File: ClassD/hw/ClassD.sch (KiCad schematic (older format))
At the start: 62 parts, among them P1 RedRCA, P2 WhiteRCA, P3 CONN_01X02, P4 CONN_01X02, P5 CONN_01X02, SW1 SW_PUSH, SW2 SW_PUSH, U1 TDA7491LP, U2 MCP1700T

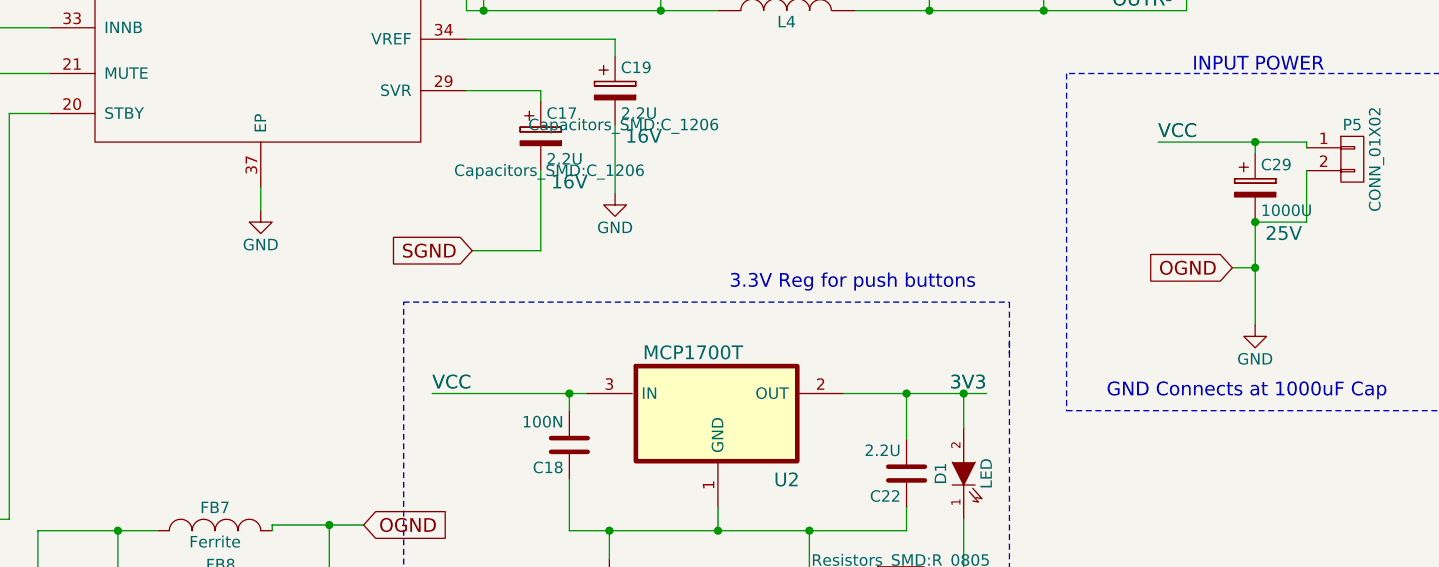
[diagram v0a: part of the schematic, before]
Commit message: Finished output filters (right side)
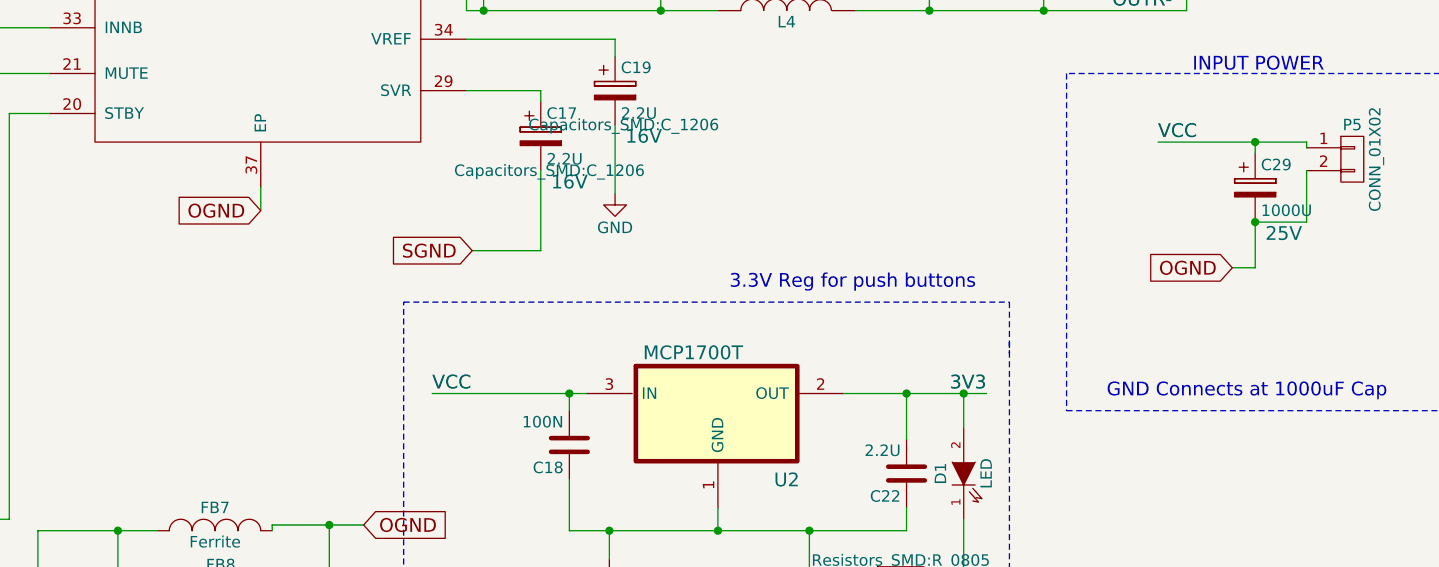
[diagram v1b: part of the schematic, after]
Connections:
- net GND: no longer C15.1, C16.2, C25.2, C26.1, C27.2, C28.1, C29.2, FB1.2, FB2.2, FB3.2, FB4.2, FB5.2, FB6.2, FB7.2, FB8.2, P5.2 (P2), U1.14 (PGNDA), U1.15 (PGNDA), U1.37 (EP), U1.4 (PGNDB), U1.5 (PGNDB)
- new net OGND: C15.1, C16.2, C25.2, C26.1, C27.2, C28.1, C29.2, FB1.2, FB2.2, FB3.2, FB4.2, FB5.2, FB6.2, FB7.2, FB8.2, P5.2 (P2), U1.14 (PGNDA), U1.15 (PGNDA), U1.37 (EP), U1.4 (PGNDB), U1.5 (PGNDB)
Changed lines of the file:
@@
 STBY
-$Comp
-L GND #PWR07
-U 1 1 56B32119
-P 5800 4650
-F 0 "#PWR07" H 5800 4400 50  0001 C CNN
-F 1 "GND" H 5800 4500 50  0000 C CNN
-F 2 "" H 5800 4650 50  0000 C CNN
-F 3 "" H 5800 4650 50  0000 C CNN
-	1    5800 4650
-	1    0    0    -1
-$EndComp
 $Comp
 L GND #PWR08
@@
 	1    0    0    -1
 $EndComp
-$Comp
-L GND #PWR09
-U 1 1 56B38442
-P 10150 5150
-F 0 "#PWR09" H 10150 4900 50  0001 C CNN
-F 1 "GND" H 10150 5000 50  0000 C CNN
-F 2 "" H 10150 5150 50  0000 C CNN
-F 3 "" H 10150 5150 50  0000 C CNN
-	1    10150 5150
-	1    0    0    -1
-$EndComp
 Text Notes 9500 5475 0    60   ~ 0
 GND Connects at 1000uF Cap
@@
 	10050 4900 10150 4900
 Wire Wire Line
-	10150 4700 10150 5150
-Wire Wire Line
 	10150 4700 10375 4700
 Wire Wire Line
 	10375 4700 10375 4475
 Connection ~ 10150 4700
-Connection ~ 10150 4900
 Wire Wire Line
 	10150 4400 10150 4350
@@
 	5175 7625 5275 7625
 Connection ~ 5175 7400
+Wire Wire Line
+	10150 4900 10150 4700
+Text GLabel 5800 4650 0    60   Input ~ 0
+OGND
 $EndSCHEMATC

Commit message: Finished layout with DRC
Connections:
- net GND: no longer U1.1 (SUB_GND)
- net OGND: now also U1.1 (SUB_GND)
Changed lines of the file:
@@
 LIBS:valves
 LIBS:ClassD
-LIBS:stm32f030c8
 LIBS:ClassD-cache
 EELAYER 25 0
@@
 $EndComp
 $Comp
-L GND #PWR01
-U 1 1 56B2E3CA
-P 4350 850
-F 0 "#PWR01" H 4350 600 50  0001 C CNN
-F 1 "GND" H 4350 700 50  0000 C CNN
-F 2 "" H 4350 850 50  0000 C CNN
-F 3 "" H 4350 850 50  0000 C CNN
-	1    4350 850
-	1    0    0    -1
-$EndComp
-$Comp
 L C C3
 U 1 1 56B2E3E6
@@
 	4875 1575 2275 1575
 Wire Wire Line
-	2275 1575 2275 1925
+	2275 1575 2275 1875
+Wire Wire Line
+	2275 1875 2275 1925
 Wire Wire Line
 	2075 1500 2075 1375
 Wire Wire Line
-	1775 1375 4875 1375
+	1775 1375 2075 1375
+Wire Wire Line
+	2075 1375 4875 1375
 Wire Wire Line
 	2275 2300 2275 2225
 Wire Wire Line
-	2075 2300 2275 2300
+	2075 2300 2175 2300
+Wire Wire Line
+	2175 2300 2275 2300
 Wire Wire Line
 	2075 2300 2075 1800
@@
 	875  2700 800  2700
 Wire Wire Line
-	4000 2000 4875 2000
+	4000 2000 4100 2000
+Wire Wire Line
+	4100 2000 4875 2000
 Wire Wire Line
 	4875 2000 4875 1975
@@
 	3700 2000 3375 2000
 Wire Wire Line
-	3375 1775 3375 2350
+	3375 1775 3375 2000
+Wire Wire Line
+	3375 2000 3375 2350
 Wire Wire Line
 	4875 1775 3375 1775
 Connection ~ 3375 2000
 Wire Wire Line
-	4100 2000 4100 2250
+	4100 2000 4100 2150
+Wire Wire Line
+	4100 2150 4100 2250
 Wire Wire Line
 	4100 2150 4350 2150
@@
 	4625 2500 4625 2725
 Wire Wire Line
-	4625 2725 4100 2725
+	4625 2725 4375 2725
+Wire Wire Line
+	4375 2725 4100 2725
 Wire Wire Line
 	4100 2725 4100 2550
@@
 	3575 3250 3575 3275
 Wire Wire Line
-	3575 3275 3800 3275
+	3575 3275 3650 3275
+Wire Wire Line
+	3650 3275 3800 3275
 Wire Wire Line
 	3800 3275 3800 3250
@@
 	3800 2925 3800 2950
 Wire Wire Line
-	3575 2925 3800 2925
+	3575 2925 3700 2925
+Wire Wire Line
+	3700 2925 3800 2925
 Wire Wire Line
 	3575 2925 3575 2950
@@
 	4425 3000 4275 3000
 Wire Wire Line
-	4275 3000 4275 3150
+	4275 3000 4275 3075
+Wire Wire Line
+	4275 3075 4275 3150
 Wire Wire Line
 	4275 3150 4425 3150
@@
 	4125 3600 4125 3525
 Wire Wire Line
-	3675 3850 3675 4225
+	3675 3850 3675 4175
+Wire Wire Line
+	3675 4175 3675 4225
 Wire Wire Line
 	3475 3800 3475 3675
@@
 	3675 4600 3675 4525
 Wire Wire Line
-	3475 4600 3675 4600
+	3475 4600 3575 4600
+Wire Wire Line
+	3575 4600 3675 4600
 Wire Wire Line
 	3475 4600 3475 4100
@@
 	4875 3850 3675 3850
 Wire Wire Line
-	3175 3675 4875 3675
+	3175 3675 3475 3675
+Wire Wire Line
+	3475 3675 4875 3675
 Wire Wire Line
 	900  4200 900  3500
@@
 	3725 5225 3725 5175
 Wire Wire Line
-	3475 5175 4400 5175
+	3475 5175 3725 5175
+Wire Wire Line
+	3725 5175 4400 5175
 Wire Wire Line
 	3175 5175 3000 5175
@@
 	3450 6050 3450 6000
 Wire Wire Line
-	3200 6000 4700 6000
+	3200 6000 3450 6000
+Wire Wire Line
+	3450 6000 4700 6000
 Wire Wire Line
 	2900 6000 2725 6000
@@
 	6825 3050 6825 2950
 Wire Wire Line
-	6700 2950 7225 2950
+	6700 2950 6825 2950
+Wire Wire Line
+	6825 2950 6975 2950
+Wire Wire Line
+	6975 2950 7225 2950
 Wire Wire Line
 	6975 2950 6975 3025
 Connection ~ 6825 2950
 Wire Wire Line
-	6975 3325 6975 3475
+	6975 3325 6975 3375
+Wire Wire Line
+	6975 3375 6975 3475
 Wire Wire Line
 	6975 3475 7025 3475
@@
 	6900 1625 6900 1700
 Wire Wire Line
-	6700 1625 7025 1625
+	6700 1625 6775 1625
+Wire Wire Line
+	6775 1625 6900 1625
+Wire Wire Line
+	6900 1625 7025 1625
 Wire Wire Line
 	6700 1725 6775 1725
@@
 Connection ~ 6900 1625
 Wire Wire Line
-	6700 2050 7225 2050
+	6700 2050 6775 2050
+Wire Wire Line
+	6775 2050 6900 2050
+Wire Wire Line
+	6900 2050 7225 2050
 Wire Wire Line
 	6700 1950 6775 1950
@@
 Connection ~ 6900 2050
 Wire Wire Line
-	9725 4350 10375 4350
+	9725 4350 10150 4350
+Wire Wire Line
+	10150 4350 10375 4350
 Wire Wire Line
 	10375 4350 10375 4375
@@
 	10150 4400 10150 4350
 Wire Wire Line
-	6700 1225 7700 1225
+	6700 1225 6950 1225
+Wire Wire Line
+	6950 1225 7675 1225
+Wire Wire Line
+	7675 1225 7700 1225
 Wire Wire Line
 	6700 1325 6950 1325
@@
 Connection ~ 7675 1225
 Wire Wire Line
-	6700 2350 7800 2350
+	6700 2350 6800 2350
+Wire Wire Line
+	6800 2350 7675 2350
+Wire Wire Line
+	7675 2350 7800 2350
 Wire Wire Line
 	6700 2350 6700 2375
@@
 $EndComp
 Wire Wire Line
-	8300 1225 9850 1225
+	8300 1225 8725 1225
+Wire Wire Line
+	8725 1225 9225 1225
+Wire Wire Line
+	9225 1225 9850 1225
 Wire Wire Line
 	8725 1225 8725 1575
@@
 	8725 1875 8725 2350
 Wire Wire Line
-	8400 2350 9850 2350
+	8400 2350 8725 2350
+Wire Wire Line
+	8725 2350 9225 2350
+Wire Wire Line
+	9225 2350 9850 2350
 Text GLabel 9450 1750 2    60   Input ~ 0
 OGND
@@
 Connection ~ 8725 1225
 Wire Wire Line
-	9225 1650 9225 1875
+	9225 1650 9225 1775
+Wire Wire Line
+	9225 1775 9225 1875
 $Comp
 L C C26
@@
 Connection ~ 7550 3775
 Wire Wire Line
-	8400 2650 9850 2650
+	8400 2650 8725 2650
+Wire Wire Line
+	8725 2650 9225 2650
+Wire Wire Line
+	9225 2650 9850 2650
 Wire Wire Line
 	8725 2650 8725 3000
@@
 	8725 3300 8725 3775
 Wire Wire Line
-	8400 3775 9850 3775
+	8400 3775 8725 3775
+Wire Wire Line
+	8725 3775 9225 3775
+Wire Wire Line
+	9225 3775 9850 3775
 Text GLabel 9450 3175 2    60   Input ~ 0
 OGND
@@
 Connection ~ 8725 2650
 Wire Wire Line
-	9225 3075 9225 3300
+	9225 3075 9225 3200
+Wire Wire Line
+	9225 3200 9225 3300
 $Comp
 L C C28
@@
 	6825 3275 6825 3375
 Wire Wire Line
-	6700 3375 6975 3375
+	6700 3375 6825 3375
+Wire Wire Line
+	6825 3375 6975 3375
 Connection ~ 6975 3375
 Connection ~ 6825 3375
@@
 	6900 2050 6900 2000
 Wire Wire Line
-	6750 2650 7800 2650
+	6750 2650 6775 2650
+Wire Wire Line
+	6775 2650 7550 2650
+Wire Wire Line
+	7550 2650 7800 2650
 Wire Wire Line
 	6750 2650 6750 2625
@@
 Connection ~ 6775 2650
 Wire Wire Line
-	6700 3775 7800 3775
+	6700 3775 6775 3775
+Wire Wire Line
+	6775 3775 7550 3775
+Wire Wire Line
+	7550 3775 7800 3775
 Wire Wire Line
 	6700 3675 6700 3775
@@
 $EndComp
 Wire Wire Line
-	6550 5450 7225 5450
+	6550 5450 7150 5450
+Wire Wire Line
+	7150 5450 7225 5450
 Wire Wire Line
 	7150 5450 7150 5525
@@
 	7150 5825 7150 6050
 Wire Wire Line
-	7150 6050 8625 6050
+	7150 6050 7325 6050
+Wire Wire Line
+	7325 6050 7800 6050
+Wire Wire Line
+	7800 6050 8200 6050
+Wire Wire Line
+	8200 6050 8625 6050
 $Comp
 L C C22
@@
 	8625 5650 8625 5450
 Wire Wire Line
-	8350 5450 8975 5450
+	8350 5450 8625 5450
+Wire Wire Line
+	8625 5450 8875 5450
+Wire Wire Line
+	8875 5450 8975 5450
 Wire Wire Line
 	8625 6050 8625 5950
@@
 $EndComp
 Wire Wire Line
-	4825 6050 5350 6050
+	4825 6050 5175 6050
+Wire Wire Line
+	5175 6050 5350 6050
 Wire Wire Line
 	4825 6050 4825 6375
@@
 OGND
 Wire Wire Line
-	6250 6025 5850 6025
+	6250 6025 6100 6025
+Wire Wire Line
+	6100 6025 5850 6025
 Wire Wire Line
 	5850 6025 5850 6050
@@
 	5875 6300 6100 6300
 Wire Wire Line
-	6100 6025 6100 7625
+	6100 6025 6100 6300
+Wire Wire Line
+	6100 6300 6100 6525
+Wire Wire Line
+	6100 6525 6100 6725
+Wire Wire Line
+	6100 6725 6100 6900
+Wire Wire Line
+	6100 6900 6100 7150
+Wire Wire Line
+	6100 7150 6100 7400
+Wire Wire Line
+	6100 7400 6100 7625
 Connection ~ 6100 6025
 Wire Wire Line
@@
 	5375 6300 5175 6300
 Wire Wire Line
-	5175 6050 5175 7625
+	5175 6050 5175 6300
+Wire Wire Line
+	5175 6300 5175 6525
+Wire Wire Line
+	5175 6525 5175 6725
+Wire Wire Line
+	5175 6725 5175 6900
+Wire Wire Line
+	5175 6900 5175 7150
+Wire Wire Line
+	5175 7150 5175 7400
+Wire Wire Line
+	5175 7400 5175 7625
 Connection ~ 5175 6050
 Wire Wire Line
@@
 Text GLabel 5800 4650 0    60   Input ~ 0
 OGND
+Text GLabel 4350 850  0    60   Input ~ 0
+OGND
 $EndSCHEMATC

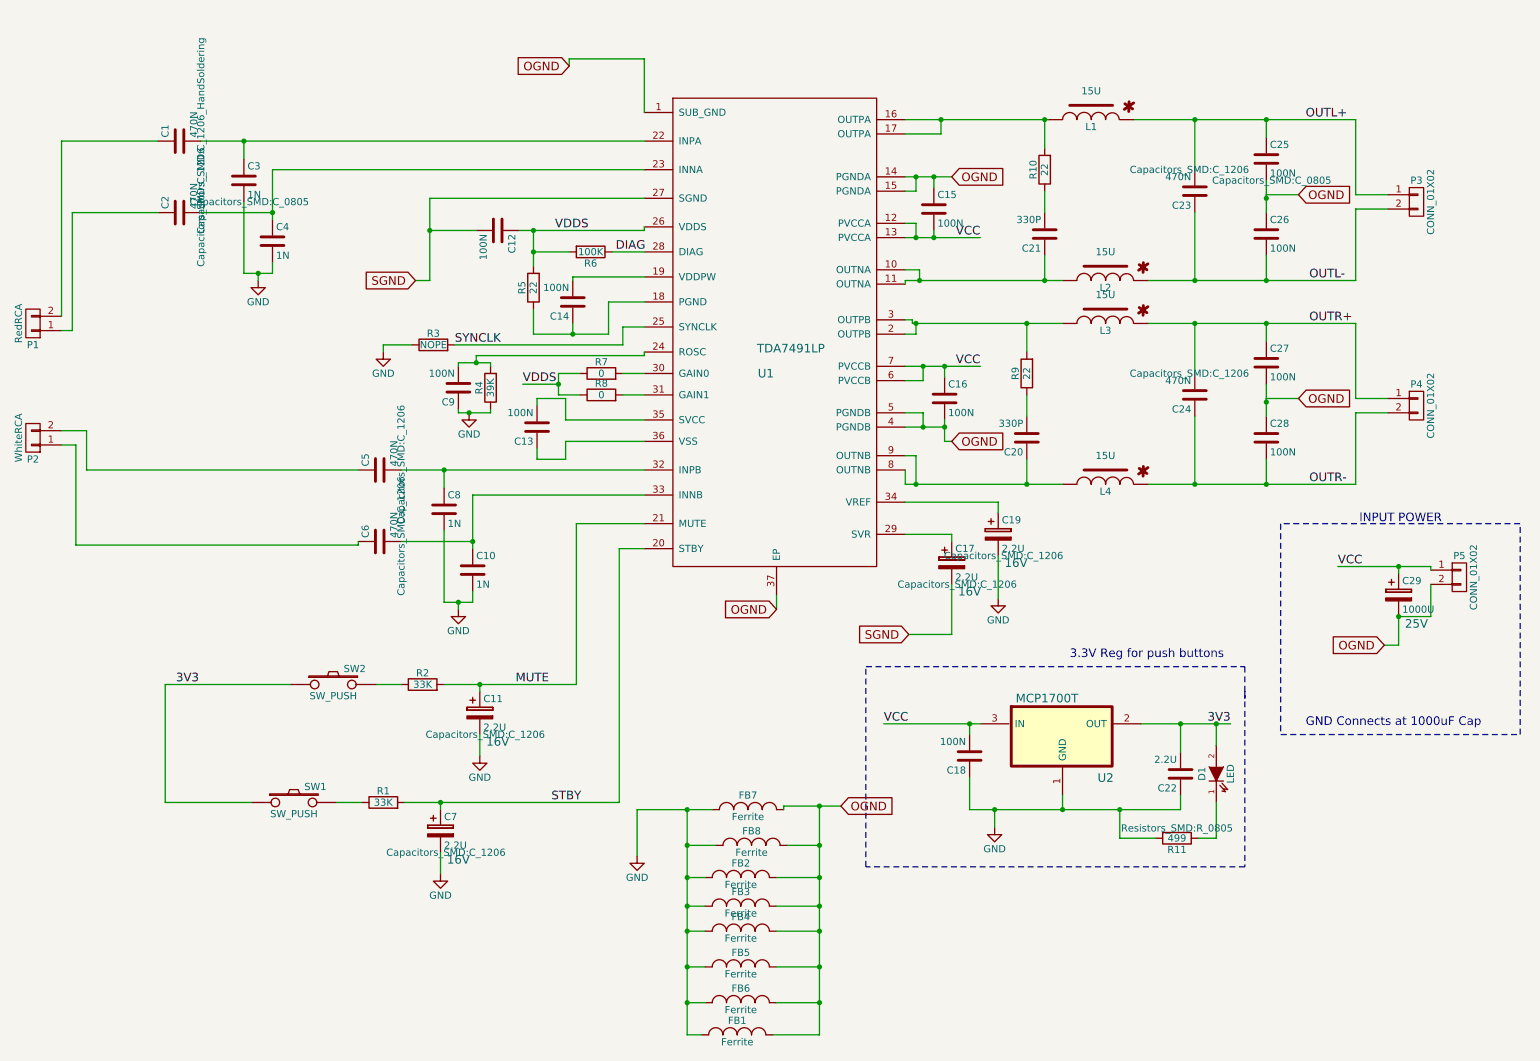
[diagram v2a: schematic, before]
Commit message: Add 2nd capacitor
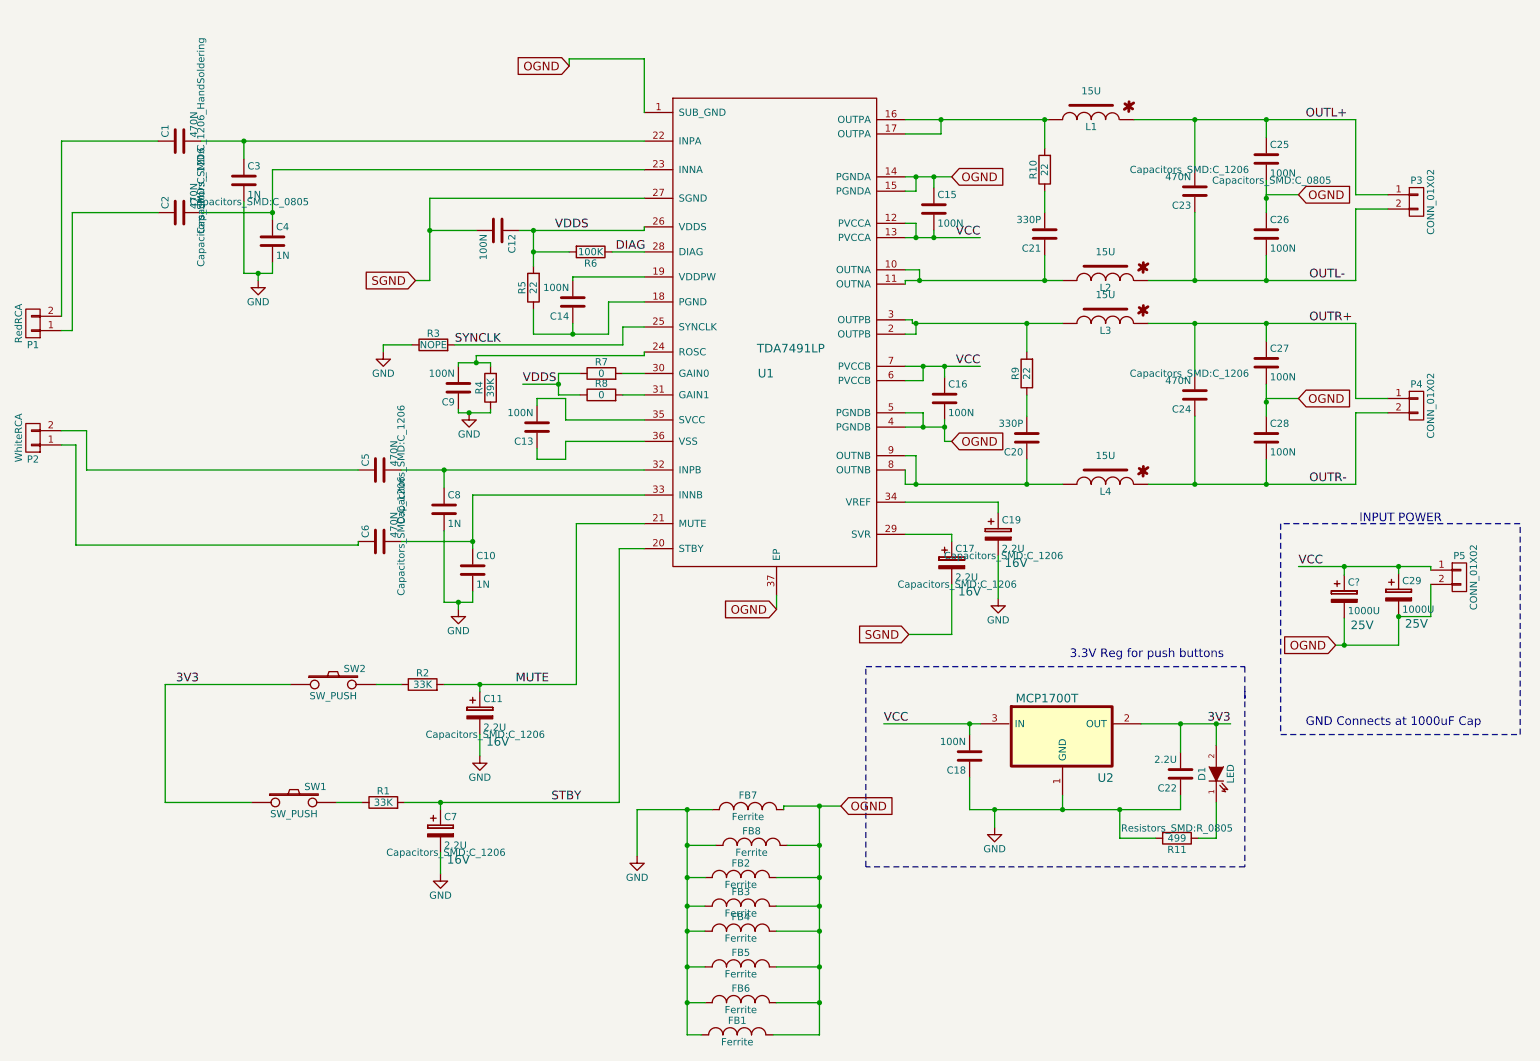
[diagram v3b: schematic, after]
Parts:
- added C?: 1000U, ClassD:c_elec_13.6x13.6, symbol CP
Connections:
- net OGND: now also C?.2
- net VCC: now also C?.1
